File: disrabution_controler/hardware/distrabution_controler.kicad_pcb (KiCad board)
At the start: 4 copper layers, 246 x 110 mm, 304 parts, among them J1 Conn_Coaxial, Q1 NMOS, Q10 PMOS, Q11 PMOS, Q12 PMOS, Q13 PMOS, Q14 PMOS, Q15 PMOS, Q16 PMOS, Q17 PMOS, Q18 PMOS, Q19 PMOS, Q2 NMOS, Q20 PMOS, Q21 NMOS, Q22 NMOS, Q23 NMOS, Q24 NMOS, Q25 NMOS, Q26 NMOS, Q27 NMOS, Q28 NMOS, Q29 NMOS, Q3 NMOS, Q30 NMOS, Q31 NMOS, Q32 NMOS, Q33 NMOS, Q34 NMOS, Q35 NMOS, Q36 NMOS, Q37 NMOS, Q4 PMOS, Q5 PMOS, Q6 PMOS, Q7 PMOS, Q8 PMOS, Q9 PMOS, U1 TJA1043T/1J, U2 ESP32-S2FH2, U3 PI4IOE5V6416LEX, U4 ECMF02-2AMX6, U5 ADS7128, U6 ADS7128, U7 AP62150WU, Y1 40 MHz

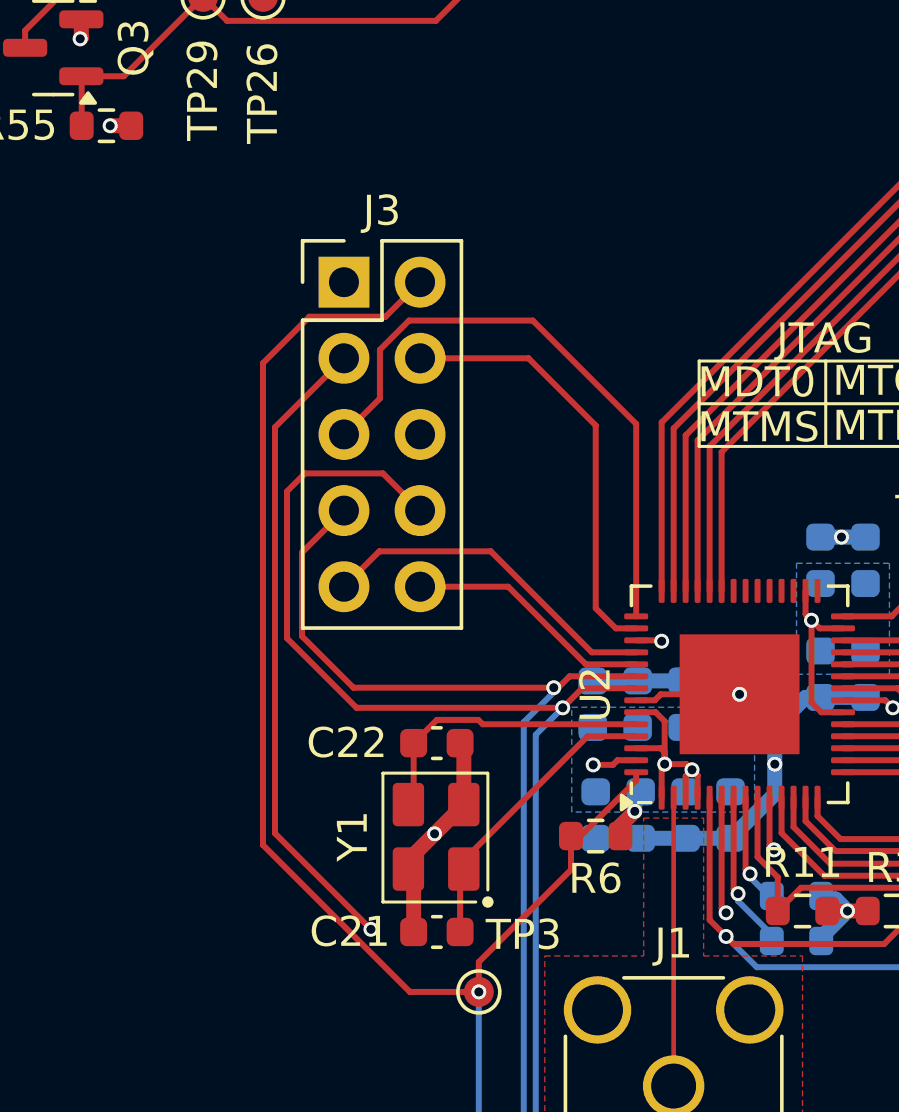
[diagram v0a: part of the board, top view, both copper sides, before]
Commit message: fixed programing connector
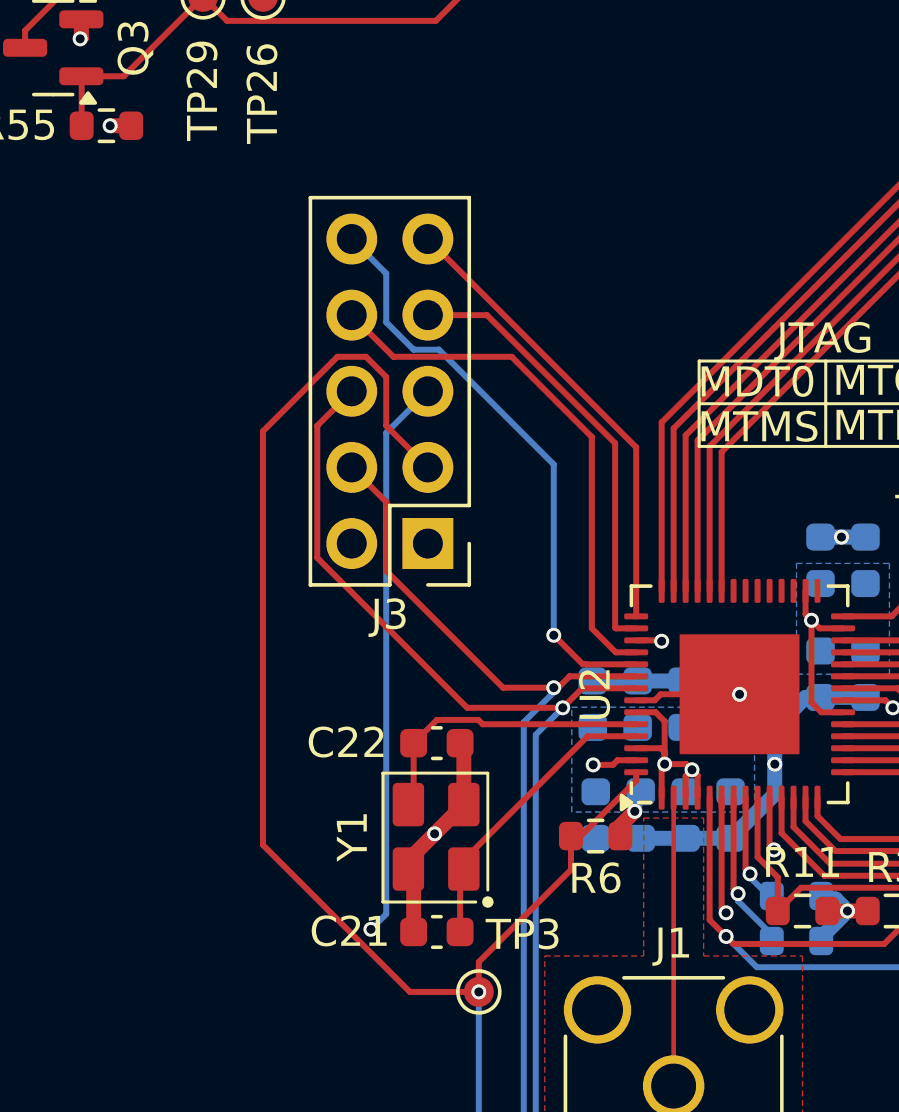
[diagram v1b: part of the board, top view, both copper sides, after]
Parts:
- moved J3 9.16 mm to (214.5, 109.2), turned to 180 degrees
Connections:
- J3 pad 2: RST -> +3V3
- J3 pad 3: ESP_IO0 -> RST
- J3 pad 4: MTD0 -> ESP_TX
- J3 pad 5: MTCK -> ESP_IO0
- J3 pad 6: +3V3 -> ESP_RX
- J3 pad 7: ESP_TX -> MTD0
- J3 pad 8: ESP_RX -> MTDI
- J3 pad 9: MTDI -> MTCK
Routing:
- net MTMS: track 8.28 -> 19.7 mm, vias 0 -> 1
- net MTDI: track 11.6 -> 17.9 mm
- net MTCK: track 20.1 -> 15.5 mm
- net ESP_RX: track 97.2 -> 93.2 mm
- net ESP_TX: track 94.3 -> 91.5 mm
- net ESP_IO0: track 85.8 -> 83.2 mm
